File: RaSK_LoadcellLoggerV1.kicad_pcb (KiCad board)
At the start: 2 copper layers, 100 x 80 mm, 41 parts, among them J1 STLINK_UART, J2 Loadcell, J3 SD_Card, J4 Mount, J5 Mount, J6 Mount, J7 Mount, P1 STLINK_SWD, SW1 TWE_RESET, SW2 TWE_PRG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

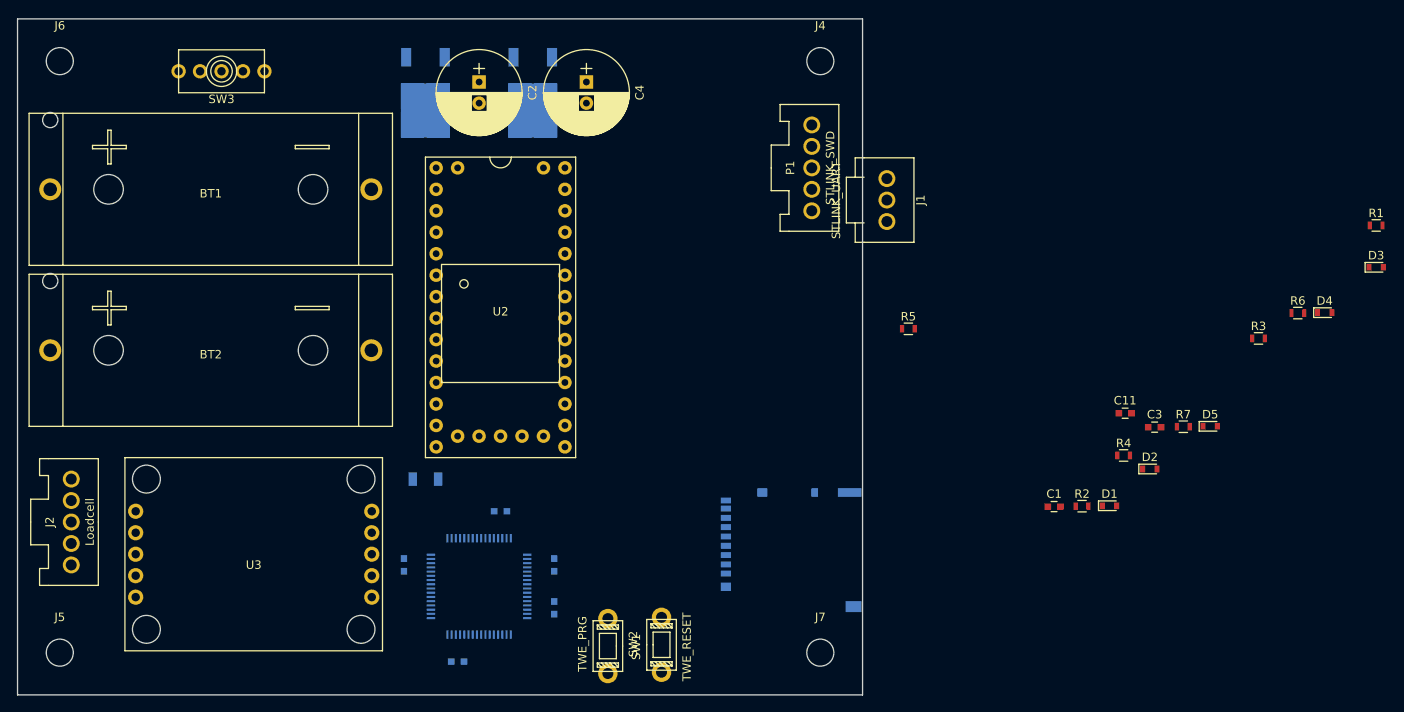
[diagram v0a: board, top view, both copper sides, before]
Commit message: create pcb file
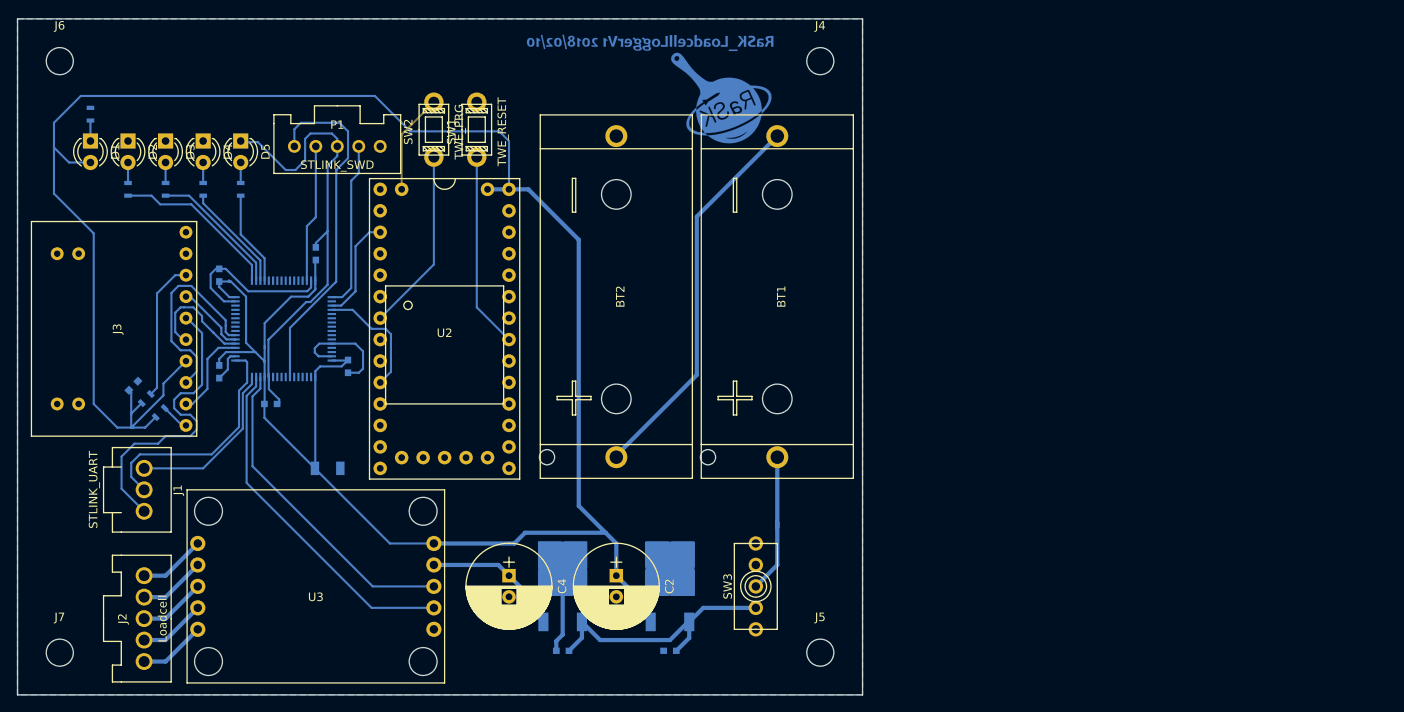
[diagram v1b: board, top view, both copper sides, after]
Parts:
- added G***: LOGO, logo:20180210, B.Cu at (154.8, 72.9)
- added G***: LOGO, logo:rask, B.Cu at (163.3, 79.2)
- C1, C11, C3, R1, R2, R3, R4, R5, R6, R7: moved to B.Cu
- D1, D2, D3, D4, D5: footprint Diodes_SMD:D_0603 -> LEDs:LED_D3.0mm
- J3: value SD_Card -> Micro_SD_Card; footprint KUT_Connector:microSD_DM3AT-SFPEJ -> KUT_Connector:AE-MICRO-SD-DIP; moved to F.Cu
- moved R1 152.7 mm to (88.6, 81.3), turned to 90 degrees
- moved D3 144.0 mm to (97.5, 84.5), turned to 270 degrees
- moved R6 136.6 mm to (95.2, 114.9), turned to 45 degrees
- moved D4 134.3 mm to (102.0, 84.5), turned to 270 degrees
- moved R3 130.5 mm to (97.5, 90.2), turned to 90 degrees
- moved D1 128.1 mm to (88.6, 84.5), turned to 270 degrees
- moved D2 127.0 mm to (93.1, 84.5), turned to 270 degrees
- moved R7 121.1 mm to (96.9, 116.6), turned to 45 degrees
- moved D5 119.6 mm to (106.4, 84.5), turned to 270 degrees
- moved R2 119.0 mm to (93.1, 90.2), turned to 90 degrees
- moved C11 117.4 mm to (93.7, 113.4), turned to 45 degrees
- moved R4 113.4 mm to (102.0, 90.2), turned to 90 degrees
- moved J1 94.4 mm to (95.0, 125.7)
- moved J5 90.0 mm to (175.0, 145.0)
- moved J7 90.0 mm to (85.0, 145.0)
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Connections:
- J3 pad 1: /SD_CS -> Net-(J3-Pad1)
- J3 pad 10: Net-(J3-Pad10) -> (no net)
- J3 pad 2: /SD_MOSI -> /SD_CS
- J3 pad 3: GND -> /SD_MOSI
- R6 pad 2: Net-(J3-Pad9) -> Net-(J3-Pad8)
- R7 pad 2: Net-(J3-Pad8) -> Net-(J3-Pad1)
- SW1 pad 1: GND -> Net-(SW1-Pad1)
- SW1 pad 2: Net-(SW1-Pad2) -> GND
- U1 pad 14: Net-(U1-Pad14) -> /LCAmp_DAT
- U1 pad 15: Net-(U1-Pad15) -> /LCAmp_SCK
- U1 pad 44: /LCAmp_SCK -> Net-(U1-Pad44)
- U1 pad 45: /LCAmp_DAT -> Net-(U1-Pad45)
- U2 pad 21: Net-(SW1-Pad2) -> Net-(SW1-Pad1)
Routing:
- net +3V3: track 0.00 -> 300.3 mm
- net GND: track 0.00 -> 148.5 mm
- net Net-(BT1-Pad2): track 0.00 -> 45.9 mm
- net /LCAmp_SCK: track 0.00 -> 41.3 mm
- net /STM_RESET: track 0.00 -> 41.2 mm
- net /LCAmp_DAT: track 0.00 -> 38.3 mm
- net +6V: track 0.00 -> 31.2 mm
- net /Debug_mIN: track 0.00 -> 27.9 mm
- net /SD_MOSI: track 0.00 -> 24.2 mm
- net Net-(SW1-Pad1): track 0.00 -> 23.2 mm
- net Net-(SW2-Pad1): track 0.00 -> 21.7 mm
- net /Debug_mOUT: track 0.00 -> 20.2 mm
- net Net-(R2-Pad1): track 0.00 -> 19.9 mm
- net /STM_SWCLK: track 0.00 -> 19.9 mm
- net Net-(BT1-Pad1): track 0.00 -> 16.9 mm
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- added copper zone on B.Cu, net GND

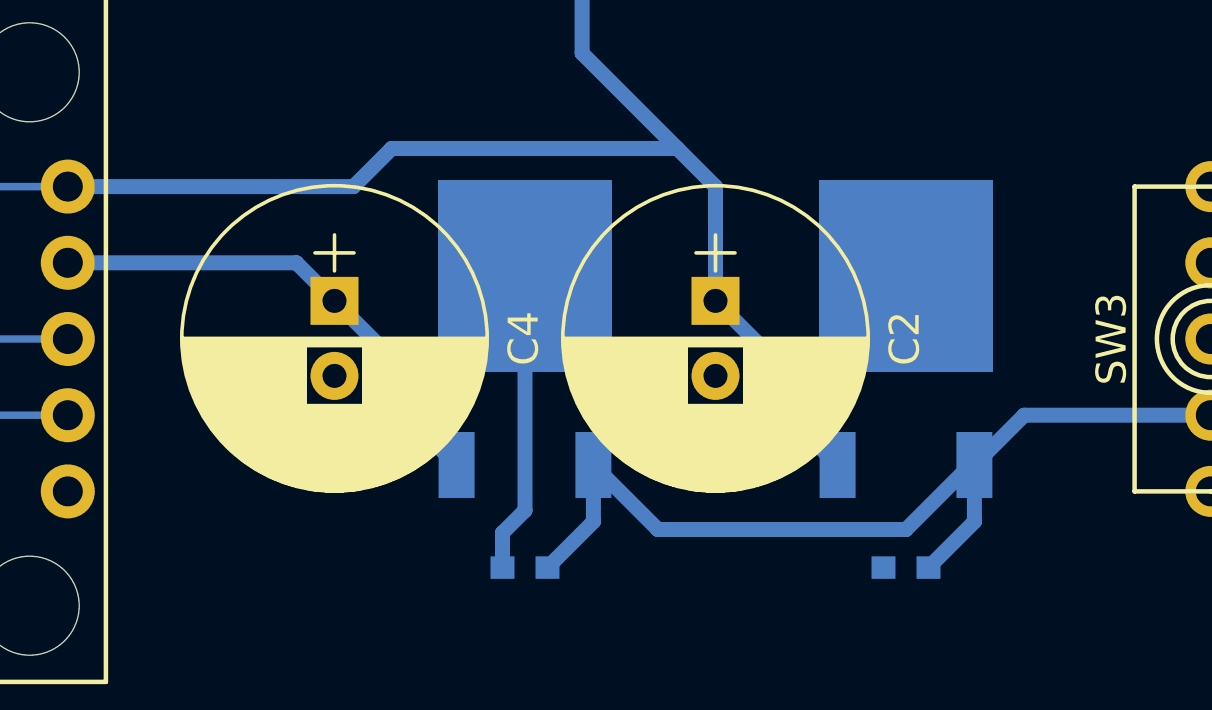
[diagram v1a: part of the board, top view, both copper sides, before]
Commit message: fix footprint of regulator and capasitor
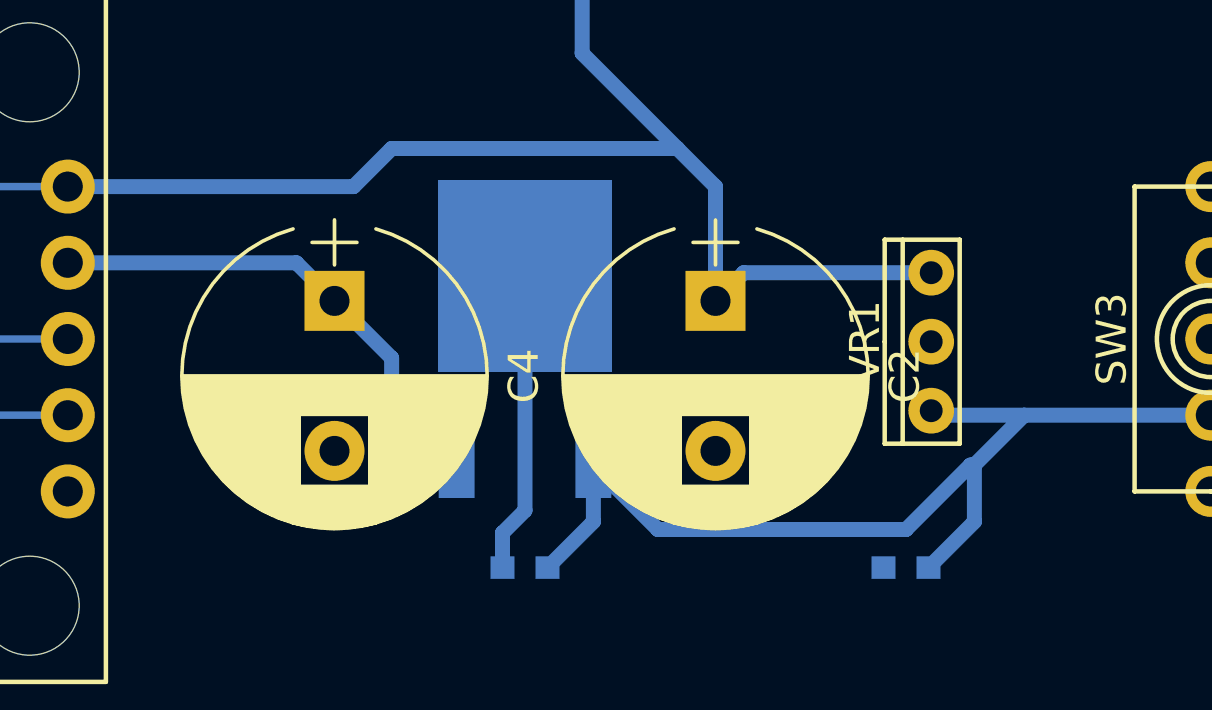
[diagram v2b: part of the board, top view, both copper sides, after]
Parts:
- C2, C4: footprint Capacitors_THT:CP_Radial_D10.0mm_P2.50mm -> Capacitors_THT:CP_Radial_D10.0mm_P5.00mm
- VR1: footprint KUT_Device:TA48Mxx -> myfootprint:HSIP3-P-2.30B; moved to F.Cu
- moved VR1 0.55 mm to (157.8, 137.2)
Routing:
- net +6V: track 31.2 -> 34.3 mm
